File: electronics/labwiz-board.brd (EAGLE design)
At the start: 98.8 x 51.3 mm, 136 parts, among them IC1 MCP3424, J1 SD_MICRO_SDIO_1BIT, J2 CORTEX_DEBUGSMD, J30 4P-SMD-2.0-90D, J4 4P-SMD-2.0-90D, J5 4P-SMD-2.0-90D, U1 STM32F10XRXT6, U4 MIC5219-3.3V, X2 M12_BOTTOM_CONTACTS_FPC_1MM, Y1 32.768kHz, Y3 32.768kHz

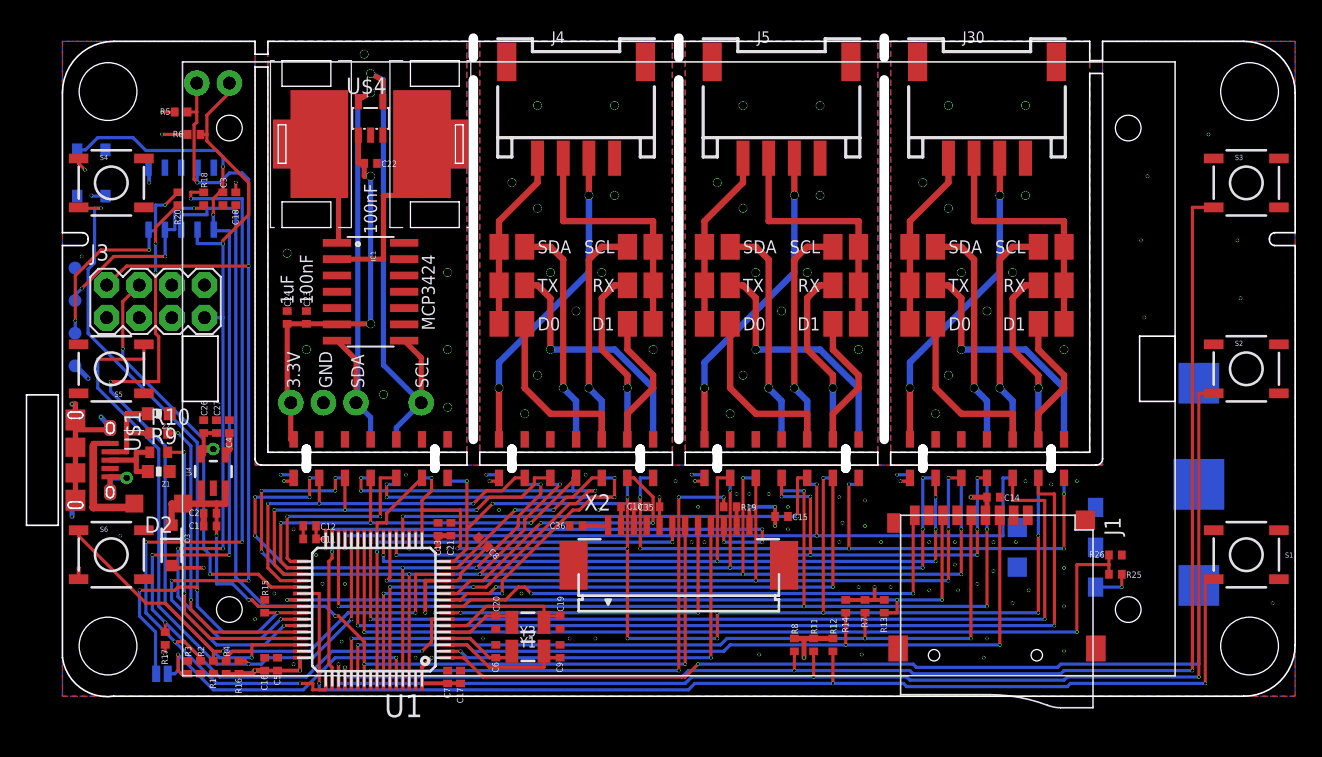
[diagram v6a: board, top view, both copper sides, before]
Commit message: Added BOOT0 jumper label. Added 100 nF caps to debounce switches.
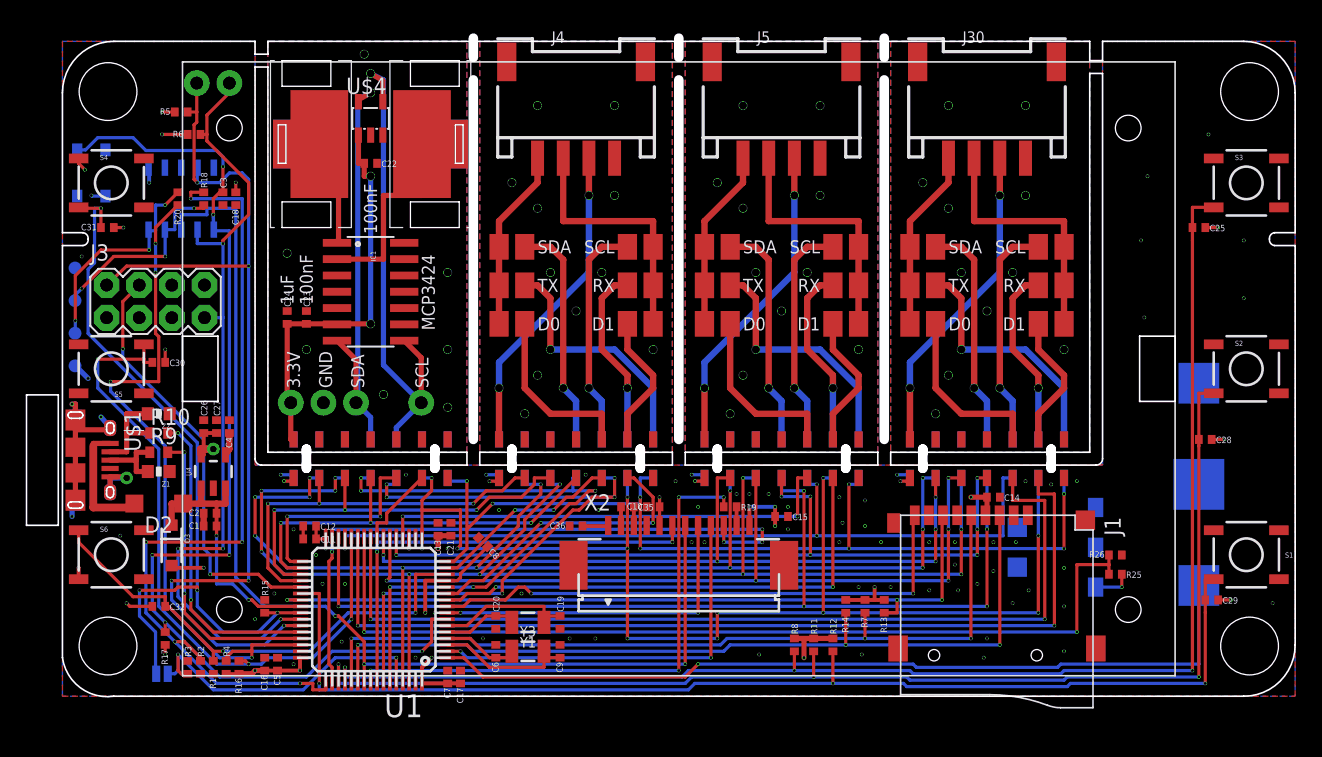
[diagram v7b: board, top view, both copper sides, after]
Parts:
- added C25, C28, C29, C30, C31, C32: 100nF, PaxInstruments-RCL:0402
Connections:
- net 3.3V: now also C31.2, C32.2
- net GND: now also C25.1, C28.1, C29.1, C30.1
- net SW_A: now also C25.2
- net SW_B: now also C28.2
- net SW_C: now also C29.2
- net SW_D_(BOOT0): now also C31.1
- net SW_E_(BOOT1): now also C30.2
- net SW_PWR_(SYS_WKUP): now also C32.1
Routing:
- net GND: track 26.7 -> 30.7 mm, vias 77 -> 81
- net 3.3V: track 65.6 -> 68.5 mm, vias 28 -> 30
- net SW_D_(BOOT0): track 59.4 -> 60.9 mm
- net SW_PWR_(SYS_WKUP): track 37.9 -> 39.1 mm
- net SW_E_(BOOT1): track 51.6 -> 52.5 mm
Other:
- board text added: "BOOT0"
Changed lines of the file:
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@@
 <setting verticaltext="up"/>
 </settings>
-<grid distance="0.25" unitdist="mm" unit="mm" style="lines" multiple="1" display="yes" altdistance="0.05" altunitdist="mil" altunit="inch"/>
+<grid distance="0.5" unitdist="mm" unit="mm" style="lines" multiple="1" display="yes" altdistance="0.05" altunitdist="mil" altunit="inch"/>
 <layers>
 <layer number="1" name="Top" color="4" fill="1" visible="yes" active="yes"/>
@@
 <text x="5.5" y="41.25" size="1" layer="22" rot="MR270">CORTEX</text>
 <text x="9.5" y="33.75" size="1" layer="22" rot="MR0">ESP8266</text>
+<text x="13.75" y="0.25" size="1" layer="22" rot="MR0">BOOT0</text>
 </plain>
 <attributes>
@@
 <element name="JP1" library="SparkFun-Passives" package="PAD-JUMPER-2-NO_YES_SILK" value="JUMPER-PAD-2-NOYES_SILK" x="7.75" y="1.75" rot="MR180"/>
 <element name="S7" library="PaxInstruments-Electromechanical" package="TACTILE_SWITCH_SMD-3" value="SWITCH-MOMENTARY-2SMD-3" x="2.25" y="40.75" rot="MR90"/>
+<element name="C25" library="PaxInstruments-RCL" package="0402" value="100nF" x="88.5" y="36.5" rot="R180"/>
+<element name="C28" library="PaxInstruments-RCL" package="0402" value="100nF" x="89" y="20" rot="R180"/>
+<element name="C29" library="PaxInstruments-RCL" package="0402" value="100nF" x="89.5" y="7.5" rot="R180"/>
+<element name="C30" library="PaxInstruments-RCL" package="0402" value="100nF" x="7.5" y="26" rot="R180"/>
+<element name="C31" library="PaxInstruments-RCL" package="0402" value="100nF" x="3.5" y="36.5"/>
+<element name="C32" library="PaxInstruments-RCL" package="0402" value="100nF" x="7.5" y="7" rot="R180"/>
 </elements>
 <signals>
@@
 <via x="8" y="3.25" extent="1-16" drill="0.2"/>
 <wire x1="8" y1="4" x2="8" y2="3.25" width="0.25" layer="1"/>
+<contactref element="C31" pad="2"/>
+<contactref element="C32" pad="2"/>
+<via x="4.75" y="36.5" extent="1-16" drill="0.2"/>
+<wire x1="4" y1="36.5" x2="4.75" y2="36.5" width="0.25" layer="1"/>
+<via x="5" y="7.25" extent="1-16" drill="0.2"/>
+<wire x1="7" y1="7" x2="5.25" y2="7" width="0.25" layer="1"/>
+<wire x1="5.25" y1="7" x2="5" y2="7.25" width="0.25" layer="1"/>
 </signal>
 <signal name="GND" class="5">
@@
 <via x="94.25" y="7.25" extent="1-16" drill="0.2"/>
 <via x="84.25" y="29.5" extent="1-16" drill="0.2"/>
-<via x="91.75" y="31" extent="1-16" drill="0.2"/>
+<via x="92" y="31" extent="1-16" drill="0.2"/>
 <via x="84" y="35.5" extent="1-16" drill="0.2"/>
-<via x="91.5" y="35.5" extent="1-16" drill="0.2"/>
+<via x="90" y="36.5" extent="1-16" drill="0.2"/>
 <via x="84.5" y="40.5" extent="1-16" drill="0.2"/>
 <via x="89.25" y="43.75" extent="1-16" drill="0.2"/>
@@
 <wire x1="3.35" y1="38.95" x2="2.3" y2="38.95" width="0.25" layer="16"/>
 <wire x1="2.3" y1="38.95" x2="2.25" y2="39" width="0.25" layer="16"/>
+<contactref element="C25" pad="1"/>
+<contactref element="C28" pad="1"/>
+<contactref element="C29" pad="1"/>
+<contactref element="C30" pad="1"/>
+<via x="92" y="35.5" extent="1-16" drill="0.2"/>
+<via x="90.5" y="20" extent="1-16" drill="0.2"/>
+<via x="91" y="7.5" extent="1-16" drill="0.2"/>
+<wire x1="90" y1="7.5" x2="91" y2="7.5" width="0.25" layer="1"/>
+<wire x1="89.5" y1="20" x2="90.5" y2="20" width="0.25" layer="1"/>
+<wire x1="89" y1="36.5" x2="90" y2="36.5" width="0.25" layer="1"/>
+<via x="8" y="27" extent="1-16" drill="0.2"/>
+<wire x1="8" y1="26" x2="8" y2="27" width="0.25" layer="1"/>
 </signal>
 <signal name="N$3">
@@
 <wire x1="7.25" y1="5" x2="7.25" y2="1.8" width="0.25" layer="16"/>
 <wire x1="7.25" y1="1.8" x2="7.3" y2="1.75" width="0.25" layer="16"/>
+<contactref element="C31" pad="1"/>
+<wire x1="3" y1="36.5" x2="3" y2="38" width="0.25" layer="1"/>
 </signal>
 <signal name="SW_B">
@@
 <via x="88.5" y="1.5" extent="1-16" drill="0.2"/>
 <wire x1="89.656" y1="23.595" x2="88.5" y2="23.595" width="0.25" layer="1"/>
-<wire x1="88.5" y1="23.595" x2="88.5" y2="1.5" width="0.25" layer="1"/>
+<wire x1="88.5" y1="23.595" x2="88.5" y2="20" width="0.25" layer="1"/>
+<contactref element="C28" pad="2"/>
+<wire x1="88.5" y1="19.5" x2="88.5" y2="1.5" width="0.25" layer="1"/>
+<wire x1="88.5" y1="20" x2="88.5" y2="19.5" width="0.25" layer="1"/>
 </signal>
 <signal name="SW_C">
@@
 <via x="60" y="1" extent="1-16" drill="0.2"/>
 <via x="89" y="1" extent="1-16" drill="0.2"/>
-<wire x1="89" y1="1" x2="89" y2="9.117" width="0.25" layer="1"/>
+<wire x1="89" y1="1" x2="89" y2="6.5" width="0.25" layer="1"/>
+<wire x1="89" y1="7.5" x2="89" y2="9.117" width="0.25" layer="1"/>
 <wire x1="89" y1="9.117" x2="89.656" y2="9.117" width="0.25" layer="1"/>
+<contactref element="C29" pad="2"/>
+<wire x1="89" y1="7.5" x2="89" y2="6.5" width="0.25" layer="1"/>
 </signal>
 <signal name="SW_A">
@@
 <via x="57" y="2" extent="1-16" drill="0.2"/>
 <via x="88" y="2" extent="1-16" drill="0.2"/>
-<wire x1="88" y1="2" x2="88" y2="38.073" width="0.25" layer="1"/>
+<wire x1="88" y1="2" x2="88" y2="35.5" width="0.25" layer="1"/>
+<wire x1="88" y1="36.5" x2="88" y2="38.073" width="0.25" layer="1"/>
 <wire x1="89.656" y1="38.073" x2="88" y2="38.073" width="0.25" layer="1"/>
+<contactref element="C25" pad="2"/>
+<wire x1="88" y1="36.5" x2="88" y2="35.5" width="0.25" layer="1"/>
 </signal>
 <signal name="USB_VCC">
@@
 <wire x1="19.25" y1="3.5" x2="12.5" y2="3.5" width="0.25" layer="16"/>
 <wire x1="12.5" y1="3.5" x2="11.75" y2="3.5" width="0.25" layer="1"/>
-<wire x1="1.264" y1="12.486" x2="1.264" y2="12.927" width="0.25" layer="1"/>
+<wire x1="1.264" y1="11.986" x2="1.264" y2="12.927" width="0.25" layer="1"/>
 <via x="12.5" y="3.5" extent="1-16" drill="0.2"/>
-<wire x1="11.75" y1="3.5" x2="8" y2="7.25" width="0.25" layer="1"/>
-<wire x1="8" y1="7.25" x2="6.5" y2="7.25" width="0.25" layer="1"/>
-<wire x1="6.5" y1="7.25" x2="1.264" y2="12.486" width="0.25" layer="1"/>
+<wire x1="8" y1="7.75" x2="5.5" y2="7.75" width="0.25" layer="1"/>
+<wire x1="5.5" y1="7.75" x2="1.264" y2="11.986" width="0.25" layer="1"/>
 <wire x1="11.75" y1="2.75" x2="11.75" y2="3.5" width="0.25" layer="1"/>
-<wire x1="1.264" y1="12.486" x2="1.25" y2="12.5" width="0.25" layer="1"/>
+<wire x1="1.264" y1="11.986" x2="1.25" y2="12.5" width="0.25" layer="1"/>
+<contactref element="C32" pad="1"/>
+<wire x1="8" y1="7.75" x2="8" y2="7" width="0.25" layer="1"/>
+<wire x1="8" y1="7" x2="8.25" y2="7" width="0.25" layer="1"/>
+<wire x1="8.25" y1="7" x2="11.75" y2="3.5" width="0.25" layer="1"/>
 </signal>
 <signal name="SWCLK">
@@
 <wire x1="14.5" y1="2.5" x2="14.25" y2="2.75" width="0.25" layer="1"/>
 <wire x1="14.25" y1="2.75" x2="13.75" y2="2.75" width="0.25" layer="1"/>
+<contactref element="C30" pad="2"/>
+<wire x1="7" y1="26" x2="6.344" y2="26" width="0.25" layer="1"/>
+<wire x1="6.344" y1="26" x2="6.344" y2="26.25" width="0.25" layer="1"/>
 </signal>
 <signal name="MOD3_GPIO1">

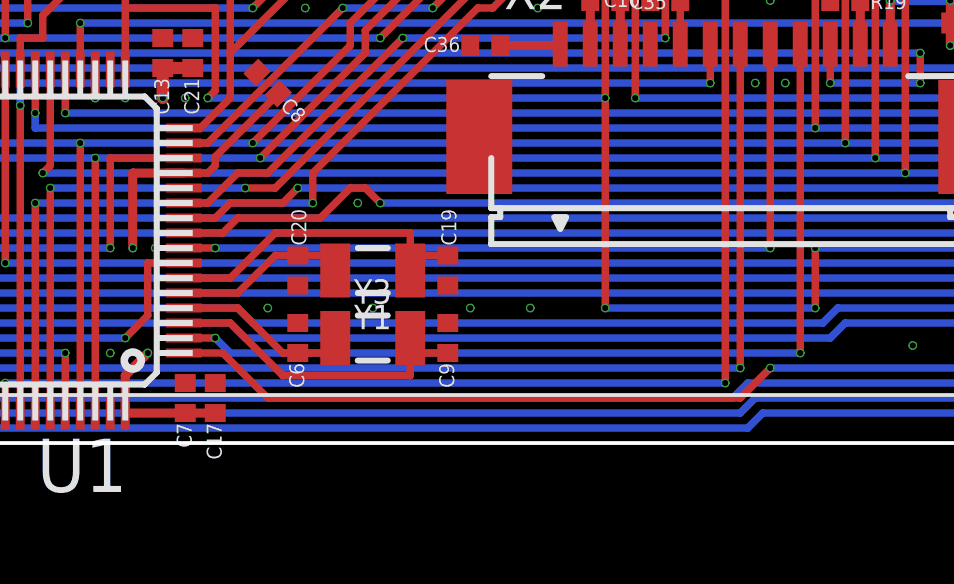
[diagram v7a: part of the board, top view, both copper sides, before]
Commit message: Swapped 8 MHz crystal for a commong footprint in HQB.
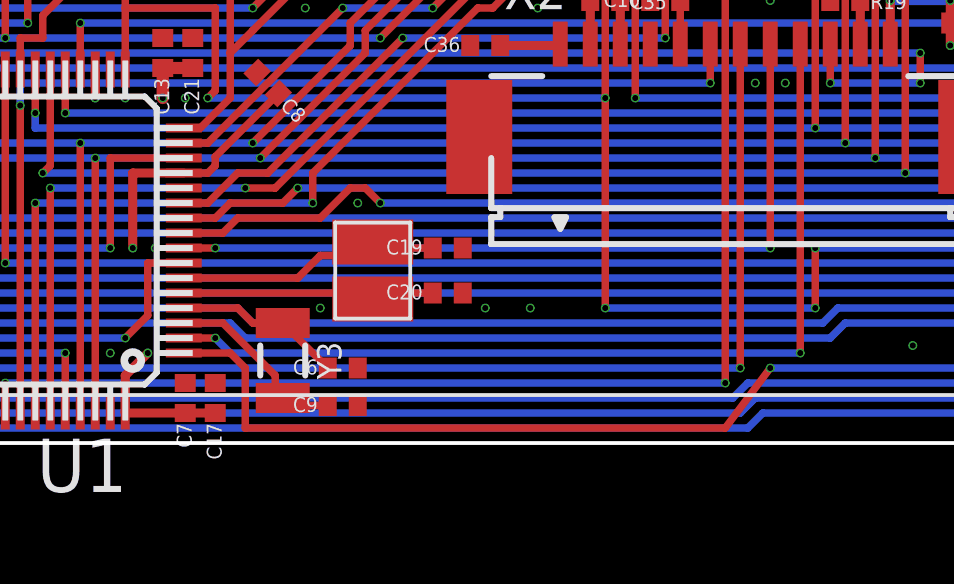
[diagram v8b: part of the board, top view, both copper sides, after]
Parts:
- removed Y1: 32.768kHz, SparkFun-FreqCtrl:CRYSTAL-SMD-3.2X1.5MM
- added U$9: NX3225GD, PaxInstruments-FreqCtrl:NX3225GD
- moved C20 5.06 mm to (38.8, 5.00), turned to 0 degrees
- moved C9 4.16 mm to (35.2, 1.25), turned to 0 degrees
- moved Y3 3.09 mm to (33.2, 2.75), turned to 270 degrees
- moved C6 1.80 mm to (35.2, 2.50), turned to 0 degrees
- moved C19 0.75 mm to (38.8, 6.50), turned to 0 degrees
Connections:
- net OSC_IN: now also U$9.P$2; no longer Y1.P$2
- net OSC_OUT: now also U$9.P$1; no longer Y1.P$1
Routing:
- net RTC_OSC_IN: track 10.8 -> 6.23 mm
- net OSC_IN: track 6.07 -> 8.47 mm
- net RTC_BAT: track 65.9 -> 68.1 mm
- net OSC_OUT: track 10.7 -> 8.88 mm
- net RTC_OSC_OUT: track 6.17 -> 5.63 mm
- net GND: vias 81 -> 80
